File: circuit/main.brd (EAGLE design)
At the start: 21.6 x 20.6 mm, 18 parts, among them IC2 LD398533RM, J1 22-27-2041-04, J2 22-27-2041-04, Q2 BSS138, Q3 12MHz, U1 ATTINY84-20SSU

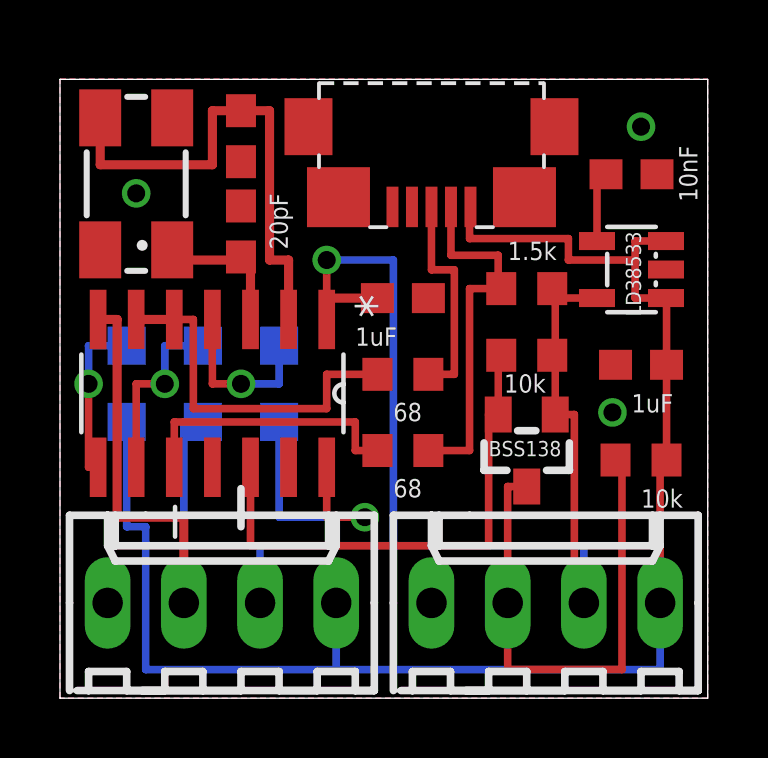
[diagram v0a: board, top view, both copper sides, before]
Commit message: Updated circuit for Shinewave v0.3.1
Signed-off-by: Garrett Greenwood <garrettagreenwood@gmail.com>
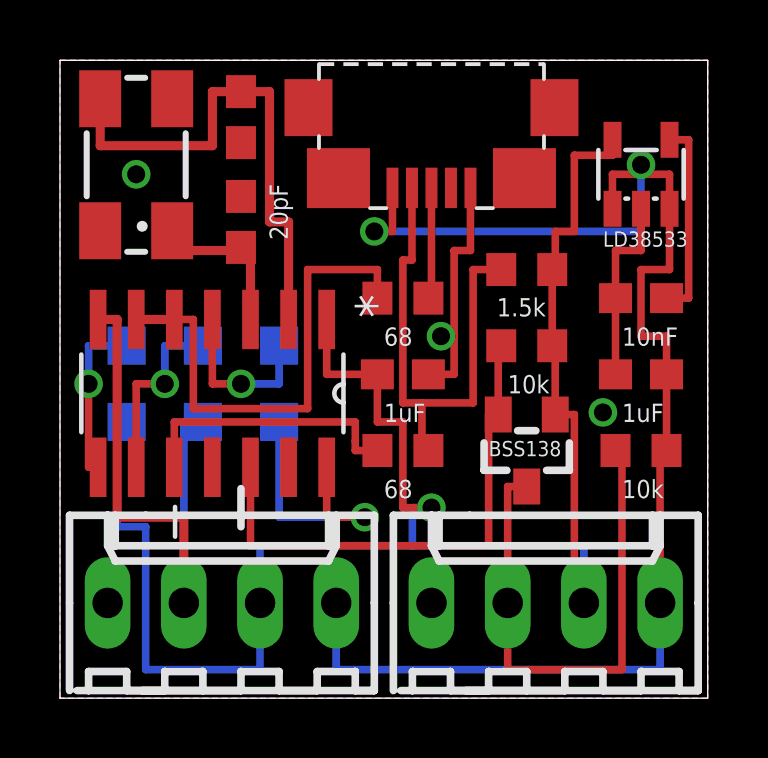
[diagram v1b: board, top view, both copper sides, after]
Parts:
- moved C1 4.14 mm to (21.0, 14.6), turned to 180 degrees
- moved IC2 3.19 mm to (21.0, 18.7), turned to 0 degrees
- moved C3 2.54 mm to (13.0, 12.1)
- moved R1 2.54 mm to (13.0, 14.6)
- moved Q3 0.64 mm to (4.13, 19.1)
- moved R3 0.63 mm to (17.1, 15.6), turned to 0 degrees
- moved C4 0.63 mm to (7.62, 20.6)
- moved U$3 0.63 mm to (14.0, 21.0)
- moved C2 0.32 mm to (21.0, 12.1)
- moved R4 0.32 mm to (17.1, 13.0)
- moved R5 0.32 mm to (21.0, 9.53)
- moved C5 0.32 mm to (7.62, 17.1)
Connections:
- removed net N$6: R2.2, R3.2, U$3.4
- new net ID: U$3.4
- new net N$2: R2.2, R3.1, U$3.2
- net 3.3V: now also R3.2, U$1.VCC; no longer R3.1
- net 5V: now also U$3.1; no longer U$1.VCC, U$3.5
- net GND: now also U$3.5; no longer U$3.1
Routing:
- net 3.3V: track 43.9 -> 61.0 mm
- net N$2: track 0.00 -> 17.0 mm
- net GND: track 8.97 -> 23.0 mm
- net N$6: track 12.1 -> 0.00 mm
- net USB_D+: track 12.2 -> 16.6 mm
- net N$4: track 2.53 -> 6.65 mm
- net 5V: track 52.2 -> 48.1 mm, vias 0 -> 2
- net N$5: track 7.21 -> 3.78 mm
- net SIG2: track 17.7 -> 18.6 mm
- net XTAL1: track 16.6 -> 17.2 mm
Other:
- board size 21.6 x 20.6 mm -> 21.6 x 21.3 mm
- board text added: "Shinewave v0.3.1"
- board text removed: "Shinewave v0.3"
